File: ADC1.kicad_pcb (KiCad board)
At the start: 2 copper layers, 21 parts, among them U8 MCP6004

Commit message: haciendo el pcb
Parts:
- added J1: Conn_01x04_Shielded, Connector_Phoenix_SPT:PhoenixContact_SPT_2.5_4-H-5.0-EX_1x04_P5.0mm_Horizontal, F.Cu at (111.0, 85.5)
- moved C45 39.6 mm to (125.0, 123.0)
- moved R55 33.0 mm to (125.0, 128.5), turned to 90 degrees
- moved R57 29.6 mm to (116.5, 128.3), turned to 90 degrees
- moved C46 27.8 mm to (111.5, 123.0)
- moved R7 26.6 mm to (125.0, 101.0)
- moved C47 25.7 mm to (111.5, 119.0)
- moved R59 23.9 mm to (112.0, 128.3), turned to -90 degrees
- moved R61 23.4 mm to (125.0, 132.3), turned to 90 degrees
- moved C40 23.1 mm to (125.0, 112.5), turned to 180 degrees
- moved R54 22.4 mm to (125.5, 106.0)
- moved R53 22.2 mm to (121.0, 128.3), turned to 90 degrees
- moved R62 21.2 mm to (116.5, 132.3), turned to 90 degrees
- moved U8 19.9 mm to (118.1, 121.5), turned to 180 degrees
- moved C16 19.4 mm to (125.1, 119.0), turned to 0 degrees
- moved D13 18.4 mm to (118.4, 112.0), turned to 0 degrees
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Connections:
- net /AV6 renamed Net-(J1-Pin_1)
- net /AV7 renamed Net-(J1-Pin_2)
- net /AV8 renamed Net-(J1-Pin_3)
- net /AV9 renamed Net-(J1-Pin_4)
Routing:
- net GND: track 20.1 -> 0.00 mm
- net /AV6_MCU: track 17.0 -> 0.00 mm
- net /AGND: track 13.0 -> 0.00 mm
- net /AV9_MCU: track 11.8 -> 0.00 mm
- net /5V: track 5.15 -> 0.00 mm
- net Net-(U8B--): track 3.31 -> 0.00 mm
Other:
- board outline added: 28 x 58 mm

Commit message: seguimos enrutando
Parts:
- moved C40 0.90 mm to (124.5, 111.8), turned to -90 degrees
- turned C46 to 180 degrees
- turned R52 to -90 degrees
- turned R56 to 90 degrees
- turned R58 to 90 degrees
- turned R59 to 90 degrees
- turned R7 to 90 degrees
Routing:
- net (no net): track 0.00 -> 86.5 mm
- net GND: track 0.00 -> 39.4 mm
- net /5V: track 0.00 -> 25.3 mm
- net Net-(RN2-R3.2): track 0.00 -> 24.5 mm
- net Net-(RN2-R1.2): track 0.00 -> 21.7 mm
- net Net-(J1-Pin_4): track 0.00 -> 14.2 mm
- net Net-(RN2-R2.2): track 0.00 -> 13.6 mm
- net Net-(J1-Pin_2): track 0.00 -> 13.2 mm
- net /AGND: track 0.00 -> 13.0 mm
- net Net-(U8B--): track 0.00 -> 8.59 mm
- net Net-(J1-Pin_3): track 0.00 -> 8.21 mm
- net Net-(U8A--): track 0.00 -> 6.53 mm
- net Net-(J1-Pin_1): track 0.00 -> 6.40 mm
- net Net-(U8D--): track 0.00 -> 5.21 mm
- net /AV9_MCU: track 0.00 -> 2.35 mm
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
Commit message: seguimos trabajando
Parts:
- J1: footprint Connector_Phoenix_SPT:PhoenixContact_SPT_2.5_4-H-5.0-EX_1x04_P5.0mm_Horizontal -> TerminalBlock_Phoenix:TerminalBlock_Phoenix_MKDS-1,5-4-5.08_1x04_P5.08mm_Horizontal
- moved J1 15.3 mm to (126.3, 84.6), turned to 180 degrees
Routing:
- net (no net): track 86.5 -> 11.7 mm
- net Net-(J1-Pin_4): track 14.2 -> 30.7 mm
- net Net-(RN2-R2.2): track 13.6 -> 4.55 mm
- net Net-(J1-Pin_2): track 13.2 -> 21.8 mm
- net /5V: track 25.3 -> 27.3 mm
- net Net-(RN2-R1.2): track 21.7 -> 22.4 mm

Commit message: se ponen pats
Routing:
- net Net-(J1-Pin_1): track 6.40 -> 61.5 mm
- net Net-(J1-Pin_2): track 21.8 -> 58.4 mm
- net GND: track 39.4 -> 8.11 mm
- net Net-(RN2-R4.2): track 0.00 -> 26.0 mm, vias 0 -> 2
- net Net-(RN2-R2.2): track 4.55 -> 26.0 mm, vias 0 -> 1
- net Net-(J1-Pin_3): track 8.21 -> 26.9 mm, vias 0 -> 1
- net /AGND: track 13.0 -> 0.00 mm
- net (no net): track 11.7 -> 0.00 mm
- net Net-(U8C--): track 0.00 -> 11.0 mm, vias 0 -> 1
- net /5V: track 27.3 -> 33.7 mm, vias 0 -> 1
- net Net-(U8B--): track 8.59 -> 9.24 mm
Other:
- board size 28 x 58 mm -> 23.8 x 56.5 mm

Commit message: seguimos con el PCB
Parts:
- added J2: Screw_Terminal_01x04, TerminalBlock_Phoenix:TerminalBlock_Phoenix_MKDS-1,5-4-5.08_1x04_P5.08mm_Horizontal, F.Cu at (111.1, 136.8)
- moved C16 6.15 mm to (124.5, 112.9)
- moved C47 6.15 mm to (110.9, 112.9)
- moved U8 6.15 mm to (117.5, 115.4)
- moved C40 6.15 mm to (123.9, 105.7)
- moved C45 6.15 mm to (124.4, 116.9)
- moved C46 6.15 mm to (110.9, 116.9)
- moved D13 6.15 mm to (117.8, 105.8)
- moved R52 6.15 mm to (111.9, 94.9)
- moved R54 6.15 mm to (124.9, 99.9)
- moved R55 6.15 mm to (124.4, 122.4)
- moved R56 6.15 mm to (111.9, 105.9)
- moved R58 6.15 mm to (111.9, 99.9)
- moved R7 6.15 mm to (124.4, 94.9)
- moved RN2 6.15 mm to (117.7, 97.0)
- moved R53 6.15 mm to (120.4, 122.2)
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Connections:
- net /AV6_MCU renamed Net-(J2-Pin_1)
- net /AV7_MCU renamed Net-(J2-Pin_2)
- net /AV8_MCU renamed Net-(J2-Pin_3)
- net /AV9_MCU renamed Net-(J2-Pin_4)
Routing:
- net Net-(J2-Pin_3): track 2.18 -> 27.7 mm
- net Net-(J2-Pin_4): track 2.35 -> 16.7 mm
- net Net-(J2-Pin_1): track 2.35 -> 16.3 mm
- net Net-(J2-Pin_2): track 2.35 -> 16.0 mm
- net Net-(J1-Pin_1): track 61.5 -> 53.4 mm
- net Net-(J1-Pin_2): track 58.4 -> 50.5 mm
- net Net-(J1-Pin_3): track 26.9 -> 20.9 mm
- net Net-(J1-Pin_4): track 30.7 -> 24.8 mm
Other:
- board size 23.8 x 56.5 mm -> 23.3 x 63.6 mm

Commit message: Continuamos con las masas
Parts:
- added REF**: JWT_A3963_1x02_P3.96mm_Vertical, Connector:JWT_A3963_1x02_P3.96mm_Vertical, F.Cu at (132.0, 113.7)
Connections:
- R60 pad 1: /AGND -> GND
- R61 pad 1: /AGND -> GND
- R62 pad 1: /AGND -> GND
- R63 pad 1: /AGND -> GND
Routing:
- net /5V: track 33.7 -> 48.2 mm, vias 1 -> 2
- net Net-(U8C--): track 11.0 -> 13.9 mm, vias 1 -> 2
- net Net-(RN2-R3.2): track 24.5 -> 27.0 mm
- net Net-(U8B--): track 9.24 -> 11.2 mm
- net Net-(J1-Pin_4): track 24.8 -> 26.2 mm
- net Net-(RN2-R4.2): track 26.0 -> 27.0 mm, vias 2 -> 4
- net Net-(J1-Pin_3): track 20.9 -> 20.5 mm, vias 1 -> 2
- net Net-(RN2-R2.2): track 26.0 -> 25.8 mm, vias 1 -> 2
- added copper zone on B.Cu, net GND
- added copper zone on F.Cu, net GND
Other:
- board size 23.3 x 63.6 mm -> 30.7 x 63.6 mm

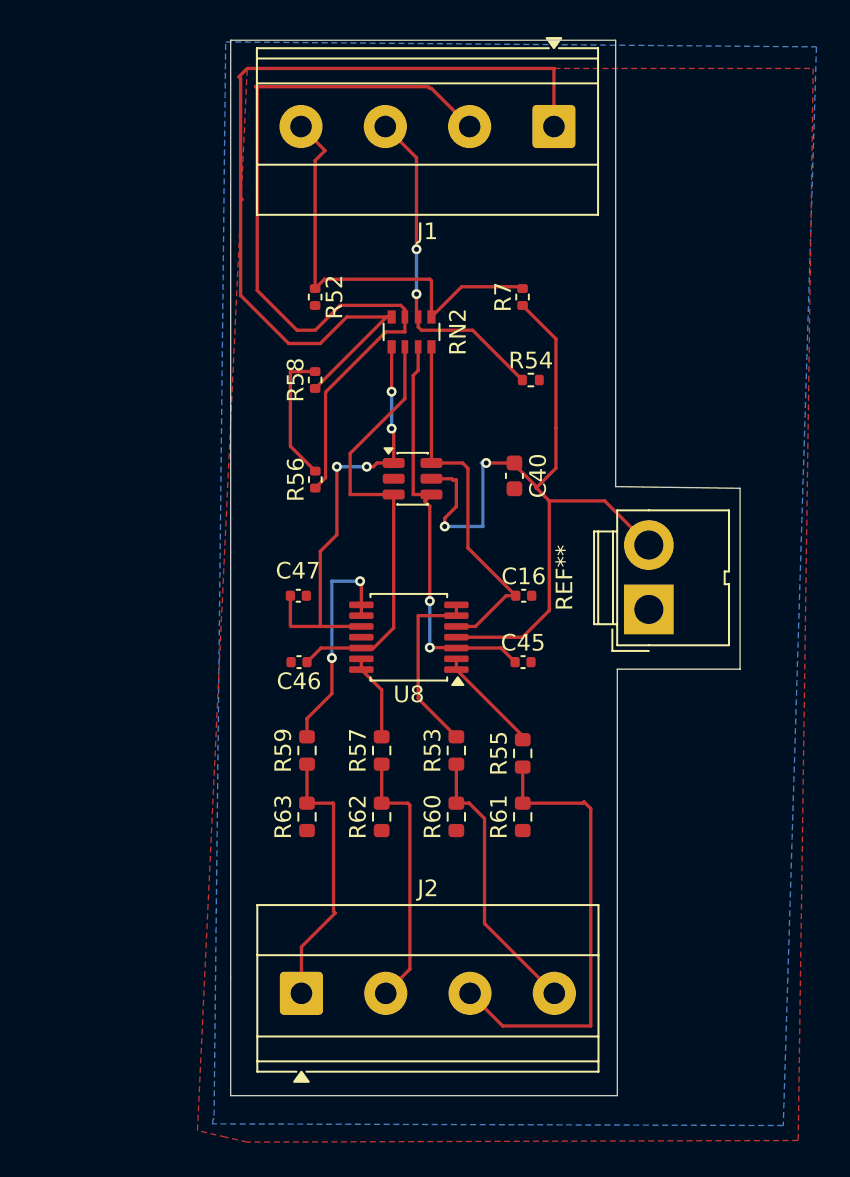
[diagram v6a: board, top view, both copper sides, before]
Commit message: cambio conjunto de resistencias de entrada
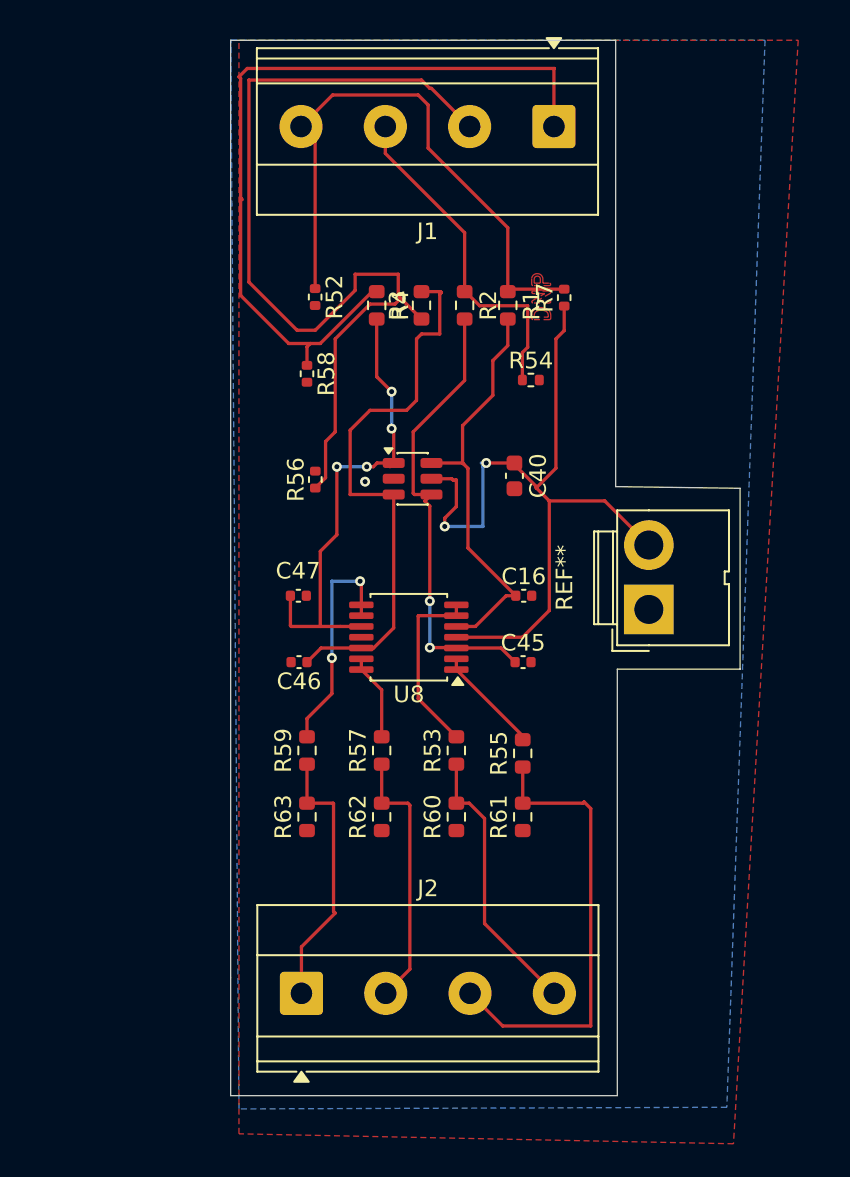
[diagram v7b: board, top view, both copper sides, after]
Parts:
- removed RN2: 10k, Resistor_SMD:R_Array_Convex_4x0603
- added R1: 10k, Resistor_SMD:R_0603_1608Metric, F.Cu at (123.5, 95.4)
- added R2: 10k, Resistor_SMD:R_0603_1608Metric, F.Cu at (120.9, 95.4)
- added R3: 10k, Resistor_SMD:R_0603_1608Metric, F.Cu at (118.3, 95.4)
- added R4: 10k, Resistor_SMD:R_0603_1608Metric, F.Cu at (115.6, 95.4)
- moved R7 2.51 mm to (126.9, 94.9)
- moved R58 0.62 mm to (111.4, 99.5), turned to -90 degrees
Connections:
- R60 pad 1: GND -> /AGND
- R61 pad 1: GND -> /AGND
- R62 pad 1: GND -> /AGND
- R63 pad 1: GND -> /AGND
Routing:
- net Net-(J1-Pin_4): track 26.2 -> 35.5 mm
- net GND: track 8.11 -> 0.00 mm, vias 0 -> 1
- net Net-(U8D-+): track 27.0 -> 34.3 mm
- net Net-(J1-Pin_2): track 50.5 -> 56.5 mm
- net Net-(J1-Pin_1): track 53.4 -> 48.2 mm
- net Net-(U8B-+): track 22.5 -> 25.4 mm
- net Net-(U8A-+): track 25.8 -> 28.6 mm
- net Net-(U8C-+): track 27.0 -> 29.1 mm
- net /5V: track 48.2 -> 47.5 mm
- net Net-(J1-Pin_3): track 20.5 -> 20.7 mm, vias 2 -> 0
